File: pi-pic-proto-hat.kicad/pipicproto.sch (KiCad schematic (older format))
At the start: 22 parts, among them J1 RUN/~PGM~, J10 Conn_01x13_Male, J2 Conn_01x02_Male, J22 Conn_01x13_Male, J3 Conn_01x02_Male, J6 Barrel_Jack_Switch, J7 Conn_01x24_Male, J8 Conn_01x06_Male, J9 Conn_01x02_Male, P1 Conn_02x20_Odd_Even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

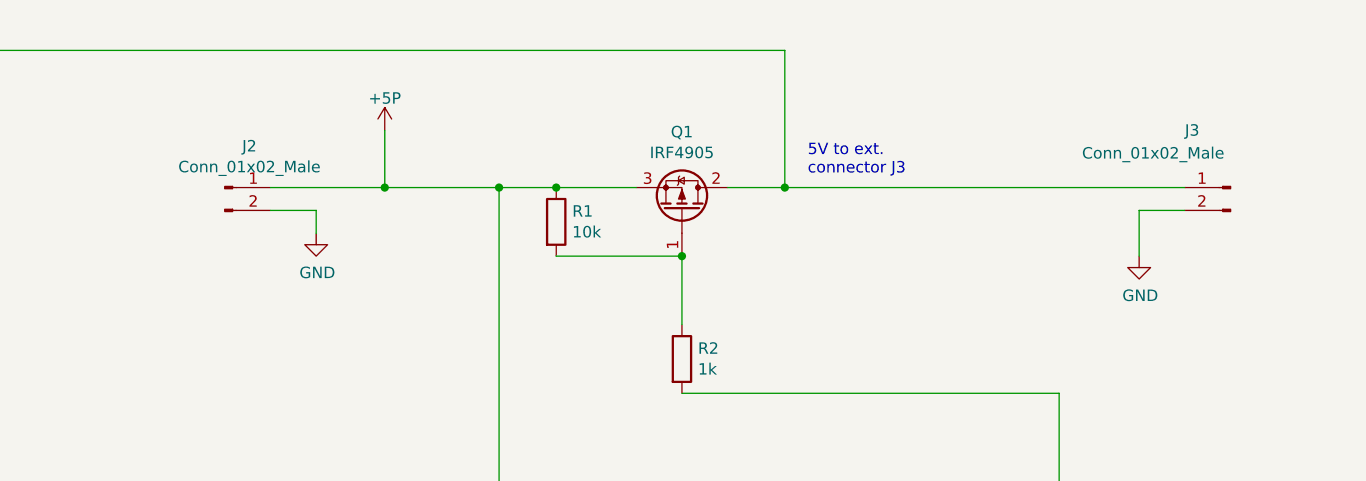
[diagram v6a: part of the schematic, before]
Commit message: V2.07: remove J2/J3 connectors
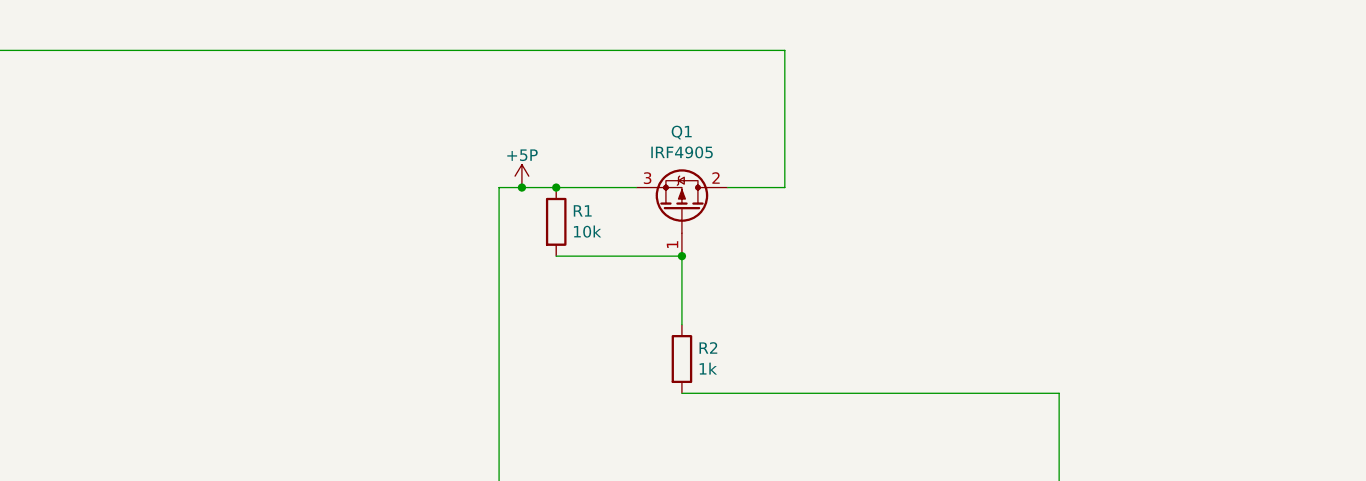
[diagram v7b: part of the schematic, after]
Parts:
- removed J2, J3: Conn_01x02_Male, Connector_Phoenix_MC:PhoenixContact_MC_1,5_2-G-3.81_1x02_P3.81mm_Horizontal, symbol Connector:Conn_01x02_Male
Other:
- note removed: "5V to ext.\nconnector J3 \n"
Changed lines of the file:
@@
 Sheet 1 1
 Title "PI PIC Prototyping Area"
-Date "2020-06-29"
-Rev "2.06"
+Date "2020-07-03"
+Rev "2.07"
 Comp "Bernhard Bablok, Lothar Hiller"
 Comment1 "https://github.com/bablokb/pi-pic-proto-hat"
@@
 	3000 1700 3000 2000
 $Comp
-L Connector:Conn_01x02_Male J2
-U 1 1 5E2DFDDC
-P 5300 1500
-F 0 "J2" H 5408 1681 50  0000 C CNN
-F 1 "Conn_01x02_Male" H 5408 1590 50  0000 C CNN
-F 2 "Connector_Phoenix_MC:PhoenixContact_MC_1,5_2-G-3.81_1x02_P3.81mm_Horizontal" H 5300 1500 50  0001 C CNN
-F 3 "~" H 5300 1500 50  0001 C CNN
-	1    5300 1500
-	1    0    0    -1
-$EndComp
-$Comp
-L Connector:Conn_01x02_Male J3
-U 1 1 5E2E091B
-P 9700 1500
-F 0 "J3" H 9900 1750 50  0000 R CNN
-F 1 "Conn_01x02_Male" H 10350 1650 50  0000 R CNN
-F 2 "Connector_Phoenix_MC:PhoenixContact_MC_1,5_2-G-3.81_1x02_P3.81mm_Horizontal" H 9700 1500 50  0001 C CNN
-F 3 "~" H 9700 1500 50  0001 C CNN
-	1    9700 1500
-	-1   0    0    -1
-$EndComp
-$Comp
 L Transistor_FET:IRF4905 Q1
 U 1 1 5E2E1286
@@
 	1    6000 4400
 	0    -1   -1   0
-$EndComp
-$Comp
-L power:GND #PWR04
-U 1 1 5E340FE7
-P 5700 1700
-F 0 "#PWR04" H 5700 1450 50  0001 C CNN
-F 1 "GND" H 5705 1527 50  0000 C CNN
-F 2 "" H 5700 1700 50  0001 C CNN
-F 3 "" H 5700 1700 50  0001 C CNN
-	1    5700 1700
-	1    0    0    -1
-$EndComp
-$Comp
-L power:GND #PWR05
-U 1 1 5E34361A
-P 9300 1800
-F 0 "#PWR05" H 9300 1550 50  0001 C CNN
-F 1 "GND" H 9305 1627 50  0000 C CNN
-F 2 "" H 9300 1800 50  0001 C CNN
-F 3 "" H 9300 1800 50  0001 C CNN
-	1    9300 1800
-	1    0    0    -1
 $EndComp
 $Comp
@@
 	7100 1500 6750 1500
 Wire Wire Line
-	6750 1500 6500 1500
+	6750 1500 6600 1500
 Connection ~ 6750 1500
-Wire Wire Line
-	6000 1250 6000 1500
-Connection ~ 6000 1500
-Wire Wire Line
-	9500 1600 9300 1600
-Wire Wire Line
-	9300 1600 9300 1800
 NoConn ~ 3950 2400
 NoConn ~ 1250 2400
@@
 	6450 3400 6250 3400
 NoConn ~ 6250 3300
-Wire Wire Line
-	5500 1500 6000 1500
-Wire Wire Line
-	5500 1600 5700 1600
-Wire Wire Line
-	5700 1600 5700 1700
 $Comp
 L Connector:Barrel_Jack_Switch J6
@@
 Wire Wire Line
 	7750 900  7750 1500
-Connection ~ 7750 1500
-Wire Wire Line
-	7750 1500 9500 1500
 $Comp
 L Connector:Conn_01x13_Male J22
@@
 	1700 5950 1450 5950
 Connection ~ 1450 5950
-Text Notes 7850 1450 0    50   ~ 0
-5V to ext.\nconnector J3 \n
 Wire Wire Line
 	8600 4700 8950 4700
@@
 Wire Wire Line
 	6500 3200 6900 3200
-Connection ~ 6500 1500
-Wire Wire Line
-	6500 1500 6000 1500
 Wire Wire Line
 	6900 3500 6900 4300
@@
 L power:+5P #PWR0103
 U 1 1 5F0543B9
-P 6000 1250
-F 0 "#PWR0103" H 6000 1100 50  0001 C CNN
-F 1 "+5P" H 6000 1390 50  0000 C CNN
-F 2 "" H 6000 1250 50  0000 C CNN
-F 3 "" H 6000 1250 50  0000 C CNN
-	1    6000 1250
+P 6600 1500
+F 0 "#PWR0103" H 6600 1350 50  0001 C CNN
+F 1 "+5P" H 6600 1640 50  0000 C CNN
+F 2 "" H 6600 1500 50  0000 C CNN
+F 3 "" H 6600 1500 50  0000 C CNN
+	1    6600 1500
 	1    0    0    -1
 $EndComp
@@
 Wire Wire Line
 	6800 4600 6800 5650
+Connection ~ 6600 1500
+Wire Wire Line
+	6600 1500 6500 1500
 $EndSCHEMATC

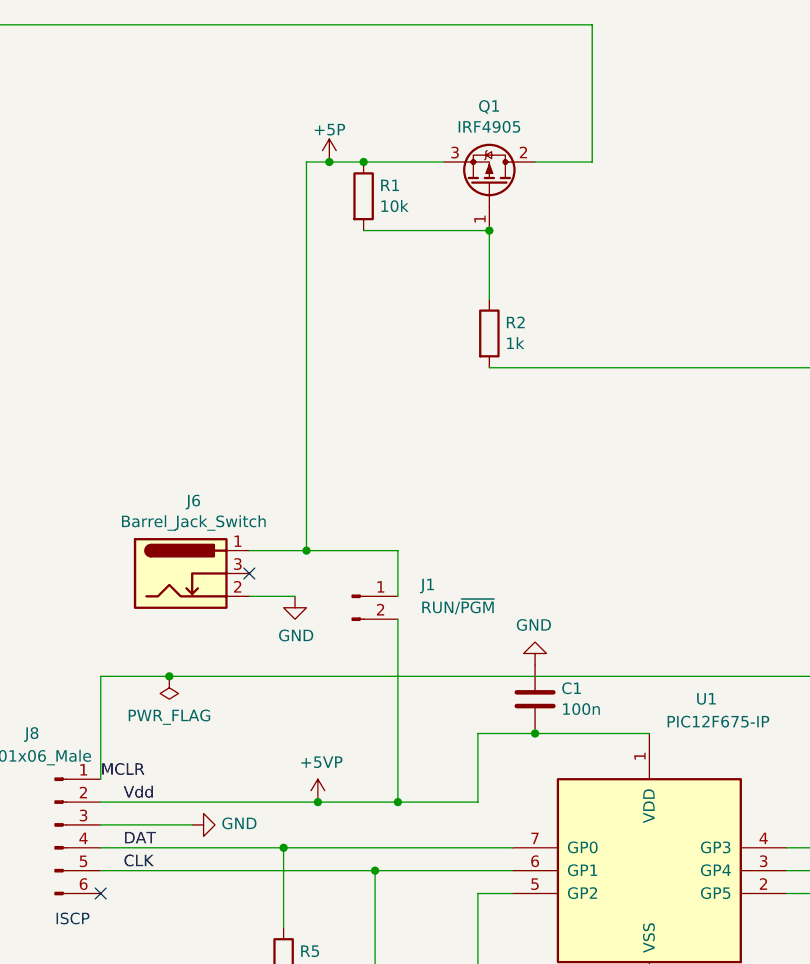
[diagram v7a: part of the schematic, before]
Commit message: V2.08: migrate to SMD for PIC
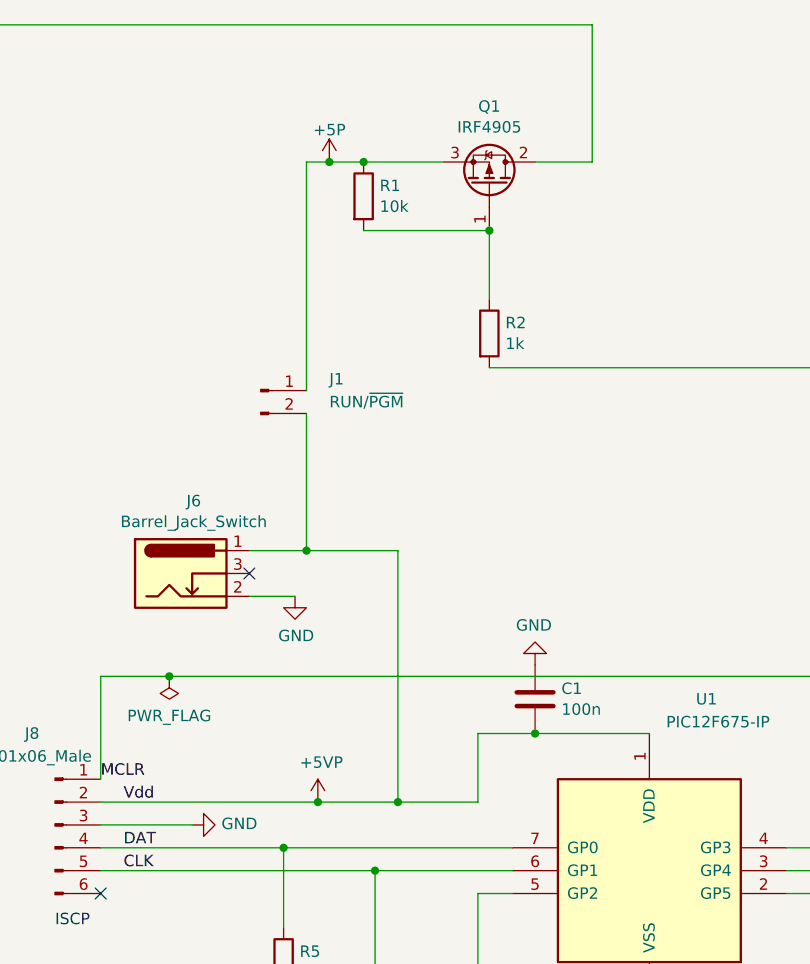
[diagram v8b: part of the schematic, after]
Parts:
- C1: footprint Capacitor_THT:C_Disc_D3.0mm_W2.0mm_P2.50mm -> Capacitor_SMD:C_1206_3216Metric_Pad1.42x1.75mm_HandSolder
- R1, R2, R5, R7, R8: footprint Resistor_THT:R_Axial_DIN0207_L6.3mm_D2.5mm_P10.16mm_Horizontal -> Resistor_SMD:R_1206_3216Metric_Pad1.42x1.75mm_HandSolder
- U1: footprint Package_DIP:DIP-8_W7.62mm -> Package_SO:SO-8_3.9x4.9mm_P1.27mm
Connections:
- net +5P: no longer J6.1
- net +5VP: now also J6.1
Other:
- moved on the sheet: J1
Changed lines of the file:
@@
 Title "PI PIC Prototyping Area"
 Date "2020-07-03"
-Rev "2.07"
+Rev "2.08"
 Comp "Bernhard Bablok, Lothar Hiller"
 Comment1 "https://github.com/bablokb/pi-pic-proto-hat"
@@
 F 0 "R2" H 7370 2296 50  0000 L CNN
 F 1 "1k" H 7370 2205 50  0000 L CNN
-F 2 "Resistor_THT:R_Axial_DIN0207_L6.3mm_D2.5mm_P10.16mm_Horizontal" V 7230 2250 50  0001 C CNN
+F 2 "Resistor_SMD:R_1206_3216Metric_Pad1.42x1.75mm_HandSolder" V 7230 2250 50  0001 C CNN
 F 3 "~" H 7300 2250 50  0001 C CNN
 	1    7300 2250
@@
 F 0 "U1" H 8250 5350 50  0000 C CNN
 F 1 "PIC12F675-IP" H 8300 5250 50  0000 C CNN
-F 2 "Package_DIP:DIP-8_W7.62mm" H 8600 5250 50  0001 C CNN
+F 2 "Package_SO:SO-8_3.9x4.9mm_P1.27mm" H 8600 5250 50  0001 C CNN
 F 3 "http://ww1.microchip.com/downloads/en/DeviceDoc/41190G.pdf" H 8000 4600 50  0001 C CNN
 	1    8000 4600
@@
 F 0 "R5" H 6470 5046 50  0000 L CNN
 F 1 "1k" H 6470 4955 50  0000 L CNN
-F 2 "Resistor_THT:R_Axial_DIN0207_L6.3mm_D2.5mm_P10.16mm_Horizontal" V 6330 5000 50  0001 C CNN
+F 2 "Resistor_SMD:R_1206_3216Metric_Pad1.42x1.75mm_HandSolder" V 6330 5000 50  0001 C CNN
 F 3 "~" H 6400 5000 50  0001 C CNN
 	1    6400 5000
@@
 F 0 "R1" H 6820 1696 50  0000 L CNN
 F 1 "10k" H 6820 1605 50  0000 L CNN
-F 2 "Resistor_THT:R_Axial_DIN0207_L6.3mm_D2.5mm_P10.16mm_Horizontal" V 6680 1650 50  0001 C CNN
+F 2 "Resistor_SMD:R_1206_3216Metric_Pad1.42x1.75mm_HandSolder" V 6680 1650 50  0001 C CNN
 F 3 "~" H 6750 1650 50  0001 C CNN
 	1    6750 1650
@@
 F 0 "C1" H 7615 3896 50  0000 L CNN
 F 1 "100n" H 7615 3805 50  0000 L CNN
-F 2 "Capacitor_THT:C_Disc_D3.0mm_W2.0mm_P2.50mm" H 7538 3700 50  0001 C CNN
+F 2 "Capacitor_SMD:C_1206_3216Metric_Pad1.42x1.75mm_HandSolder" H 7538 3700 50  0001 C CNN
 F 3 "~" H 7500 3850 50  0001 C CNN
 	1    7500 3850
@@
 L Connector:Conn_01x02_Male J1
 U 1 1 5E41F5B6
-P 6700 3400
-F 0 "J1" H 7000 3450 50  0000 L CNN
-F 1 "RUN/~PGM~" H 7000 3350 50  0000 L CNN
-F 2 "Connector_PinHeader_2.54mm:PinHeader_1x02_P2.54mm_Vertical" H 6700 3400 50  0001 C CNN
-F 3 "~" H 6700 3400 50  0001 C CNN
-	1    6700 3400
+P 6300 2500
+F 0 "J1" H 6600 2550 50  0000 L CNN
+F 1 "RUN/~PGM~" H 6600 2450 50  0000 L CNN
+F 2 "Connector_PinHeader_2.54mm:PinHeader_1x02_P2.54mm_Vertical" H 6300 2500 50  0001 C CNN
+F 3 "~" H 6300 2500 50  0001 C CNN
+	1    6300 2500
 	1    0    0    -1
 $EndComp
@@
 F 0 "R7" V 5643 5650 50  0000 C CNN
 F 1 "6.2k" V 5734 5650 50  0000 C CNN
-F 2 "Resistor_THT:R_Axial_DIN0207_L6.3mm_D2.5mm_P10.16mm_Horizontal" V 5780 5650 50  0001 C CNN
+F 2 "Resistor_SMD:R_1206_3216Metric_Pad1.42x1.75mm_HandSolder" V 5780 5650 50  0001 C CNN
 F 3 "~" H 5850 5650 50  0001 C CNN
 	1    5850 5650
@@
 F 0 "R8" H 5570 6046 50  0000 L CNN
 F 1 "12k" H 5570 5955 50  0000 L CNN
-F 2 "Resistor_THT:R_Axial_DIN0207_L6.3mm_D2.5mm_P10.16mm_Horizontal" V 5430 6000 50  0001 C CNN
+F 2 "Resistor_SMD:R_1206_3216Metric_Pad1.42x1.75mm_HandSolder" V 5430 6000 50  0001 C CNN
 F 3 "~" H 5500 6000 50  0001 C CNN
 	1    5500 6000
@@
 Text Notes 9350 4150 1    50   ~ 0
 GP2
-Connection ~ 6900 4300
-Wire Wire Line
-	6900 4300 7250 4300
-Wire Wire Line
-	6900 3400 6900 3200
 Wire Wire Line
 	3250 900  7750 900
 Connection ~ 6550 4300
-Wire Wire Line
-	6550 4300 6900 4300
-Wire Wire Line
-	6250 3200 6500 3200
-Wire Wire Line
-	6500 3200 6500 1500
-Connection ~ 6500 3200
-Wire Wire Line
-	6500 3200 6900 3200
-Wire Wire Line
-	6900 3500 6900 4300
 Wire Wire Line
 	5600 3750 5900 3750
@@
 Wire Wire Line
 	6600 1500 6500 1500
+Wire Wire Line
+	6250 3200 6500 3200
+Wire Wire Line
+	6500 1500 6500 2500
+Wire Wire Line
+	6500 2600 6500 3200
+Connection ~ 6500 3200
+Wire Wire Line
+	6500 3200 6900 3200
+Wire Wire Line
+	6550 4300 6900 4300
+Wire Wire Line
+	6900 4300 7250 4300
+Connection ~ 6900 4300
+Wire Wire Line
+	6900 3200 6900 4300
 $EndSCHEMATC
